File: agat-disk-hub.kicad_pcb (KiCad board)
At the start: 2 copper layers, 53.3 x 61 mm, 18 parts, among them J1 IDC‐20, J2 IDC‐20, J3 IDC‐34, J4 IDC‐10, J5 KK‐4

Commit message: remove -12|DE2 option with JP1, rename JP3 to JP1 and move to its old place; label JP2 as FW307
The option of supplying DE2 via +12 wire on IDC-20 or Eltra is considered dangerous for controllers
(if someone plugs a standard cable with -12 into our board with this jumper on), so it is removed
together with its JP1; the Net -12|DE renamed to just -12.

JP3 (jumper parking ground) is renamed to JP1 and moved to the place previously occupied by JP1.

Other minor adjustments:
- Adjust a few J3 traces.
- Adjust silk items, including:
  - The "jumper parking" label made bigger, as a regular Function front-side label.
  - The "(FW 307)" label at JP2 becomes its Function on the Schematics and now reads "FW307".
  - Remove back side brackets for XP1 and J1.
  - Center horitontal labels by their coordinate, not by the visually occupied space.
  - Make the text of knocked-out labels bolder.
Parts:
- removed the JP1 at (96.4, 89.1)
- moved JP1 33.0 mm to (96.4, 89.1), turned to -90 degrees
- moved G*** 0.14 mm to (52.2, 97.9)
- renumbered JP3 to JP1
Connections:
- net /-12|DE2 renamed /-12
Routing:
- net /-12: track 52.7 -> 36.2 mm
- net /DE2: track 103.5 -> 93.4 mm
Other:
- board text added: "-12"
- board text added: "Ф1C→G.32"
- board text removed: "-12|DE2"

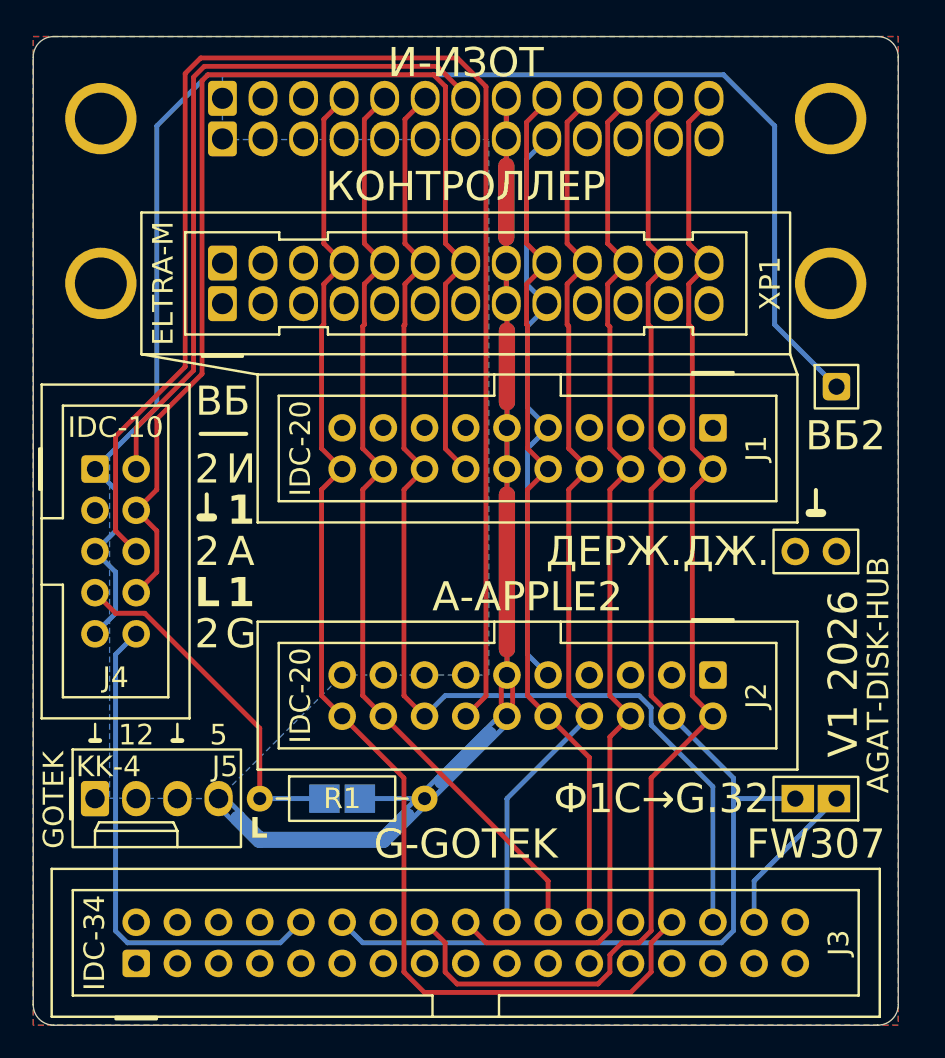
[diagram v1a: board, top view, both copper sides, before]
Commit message: remove thermal reliefs on 1 mm +5 trace
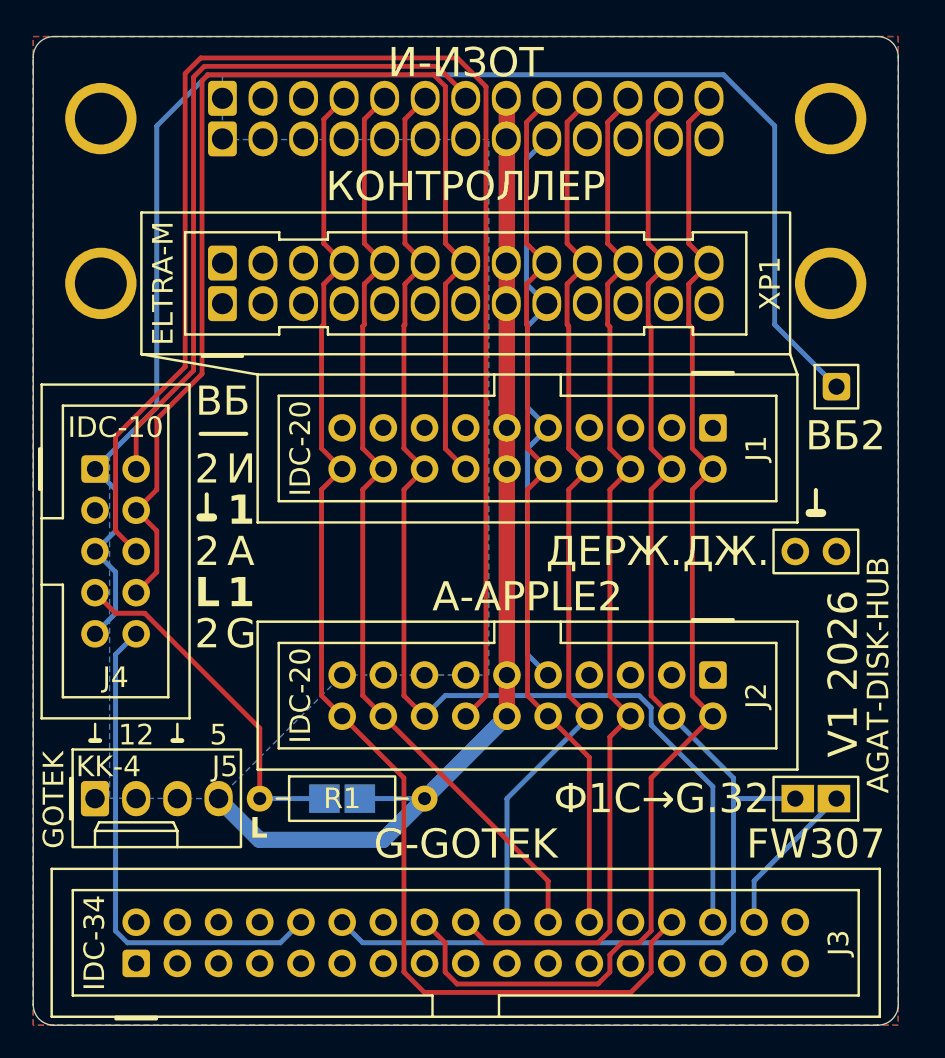
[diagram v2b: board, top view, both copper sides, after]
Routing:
- net /+5: track 110.1 -> 99.7 mm
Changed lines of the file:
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@@
 	)
 	(segment
-		(start 76.08 63.72)
-		(end 76.12 63.76)
-		(width 0.3)
-		(layer "F.Cu")
-		(net "/+5")
-	)
-	(segment
-		(start 76.08 69.77)
-		(end 76.08 65.34)
+		(start 76.12 61.22)
+		(end 76.12 99.28)
 		(width 1)
 		(layer "F.Cu")
@@
 	)
 	(segment
-		(start 76.12 96.74)
-		(end 76.12 95.16)
-		(width 0.3)
-		(layer "F.Cu")
-		(net "/+5")
-	)
-	(segment
-		(start 76.08 73.89)
-		(end 76.08 69.77)
-		(width 0.3)
-		(layer "F.Cu")
-		(net "/+5")
-	)
-	(segment
-		(start 76.12 85.61)
-		(end 76.12 95.16)
+		(start 76.08 61.18)
+		(end 76.12 61.22)
 		(width 1)
 		(layer "F.Cu")
@@
 	)
 	(segment
-		(start 76.12 79.93)
-		(end 76.12 85.61)
-		(width 0.3)
-		(layer "F.Cu")
+		(start 58.34 104.38)
+		(end 60.86 106.9)
+		(width 1)
+		(layer "B.Cu")
 		(net "/+5")
 	)
 	(segment
-		(start 76.47 99.28)
-		(end 76.47 96.74)
-		(width 0.3)
-		(layer "F.Cu")
+		(start 58.34 104.36)
+		(end 58.34 104.38)
+		(width 1)
+		(layer "B.Cu")
 		(net "/+5")
 	)
 	(segment
-		(start 76.24 63)
-		(end 76.08 63.16)
-		(width 0.3)
-		(layer "F.Cu")
-		(net "/+5")
-	)
-	(segment
-		(start 76.08 61.22)
-		(end 76.08 65.34)
-		(width 0.3)
-		(layer "F.Cu")
-		(net "/+5")
-	)
-	(segment
-		(start 76.12 79.93)
-		(end 76.12 75.5)
-		(width 1)
-		(layer "F.Cu")
-		(net "/+5")
-	)
-	(segment
-		(start 76.12 73.89)
-		(end 76.12 75.5)
-		(width 0.3)
-		(layer "F.Cu")
-		(net "/+5")
-	)
-	(segment
-		(start 76.08 63.16)
-		(end 76.08 63.72)
-		(width 0.3)
-		(layer "F.Cu")
-		(net "/+5")
-	)
-	(segment
-		(start 75.77 99.28)
-		(end 75.77 96.74)
-		(width 0.3)
-		(layer "F.Cu")
-		(net "/+5")
-	)
-	(segment
-		(start 76.08 73.89)
-		(end 76.08 69.77)
+		(start 67.05 104.36)
+		(end 71.04 104.36)
 		(width 0.3)
 		(layer "B.Cu")
@@
 	)
 	(segment
-		(start 68.5 106.9)
-		(end 69.96 105.44)
+		(start 76.08 61.18)
+		(end 76.12 61.22)
 		(width 1)
-		(layer "B.Cu")
-		(net "/+5")
-	)
-	(segment
-		(start 76.12 85.61)
-		(end 76.12 95.16)
-		(width 1)
-		(layer "B.Cu")
-		(net "/+5")
-	)
-	(segment
-		(start 58.685 104.235)
-		(end 59.795 105.345)
-		(width 0.3)
 		(layer "B.Cu")
 		(net "/+5")
@@
 	)
 	(segment
-		(start 76.12 96.74)
-		(end 76.12 95.16)
-		(width 0.3)
-		(layer "B.Cu")
-		(net "/+5")
-	)
-	(segment
-		(start 67.05 104.36)
-		(end 71.04 104.36)
-		(width 0.3)
-		(layer "B.Cu")
-		(net "/+5")
-	)
-	(segment
-		(start 76.12 79.93)
-		(end 76.12 85.61)
-		(width 0.3)
-		(layer "B.Cu")
-		(net "/+5")
-	)
-	(segment
-		(start 74.765 100.145)
-		(end 75.875 99.035)
-		(width 0.3)
-		(layer "B.Cu")
-		(net "/+5")
-	)
-	(segment
-		(start 58.195 104.725)
-		(end 59.305 105.835)
-		(width 0.3)
-		(layer "B.Cu")
-		(net "/+5")
-	)
-	(segment
-		(start 69.54 105.37)
-		(end 72.035 102.875)
-		(width 0.3)
-		(layer "B.Cu")
-		(net "/+5")
-	)
-	(segment
-		(start 59.55 105.59)
-		(end 60.86 106.9)
+		(start 68.5 106.9)
+		(end 76.12 99.28)
 		(width 1)
 		(layer "B.Cu")
@@
 	)
 	(segment
-		(start 76.08 69.77)
-		(end 76.08 65.34)
+		(start 76.12 61.22)
+		(end 76.12 96.74)
 		(width 1)
 		(layer "B.Cu")
 		(net "/+5")
-	)
-	(segment
-		(start 75.255 100.635)
-		(end 76.365 99.525)
-		(width 0.3)
-		(layer "B.Cu")
-		(net "/+5")
-	)
-	(segment
-		(start 69.945 105.945)
-		(end 72.525 103.365)
-		(width 0.3)
-		(layer "B.Cu")
-		(net "/+5")
-	)
-	(segment
-		(start 76.08 61.22)
-		(end 76.08 65.34)
-		(width 0.3)
-		(layer "B.Cu")
-		(net "/+5")
-	)
-	(segment
-		(start 72.12 103.28)
-		(end 75.01 100.39)
-		(width 1)
-		(layer "B.Cu")
-		(net "/+5")
-	)
-	(segment
-		(start 76.12 79.93)
-		(end 76.12 75.5)
-		(width 1)
-		(layer "B.Cu")
-		(net "/+5")
-	)
-	(segment
-		(start 76.12 73.89)
-		(end 76.12 75.5)
-		(width 0.3)
-		(layer "B.Cu")
-		(net "/+5")
